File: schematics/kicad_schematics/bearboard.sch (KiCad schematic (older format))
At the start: 86 parts, among them P1 KOBICONN, P10 CONN_4, P11 CONN_10X2, P2 CONN_10X2, P3 CONN_10X2, P4 CONN_10X2, P5 CONN_10X2, P6 CONN_10X2, P7 CONN_10X2, P8 CONN_10X2, P9 CONN_7, SW1 SW_PUSH, SW5 SWITCH, SW6 SWITCH, U1 VBAT, U14 SD_CARD, U2 STM32F103, U3 TACT-SKQU, U4 EMA406GPS, X1 8-16MHz, X2 32.768KHz, X3 ARDUINOSHIELD

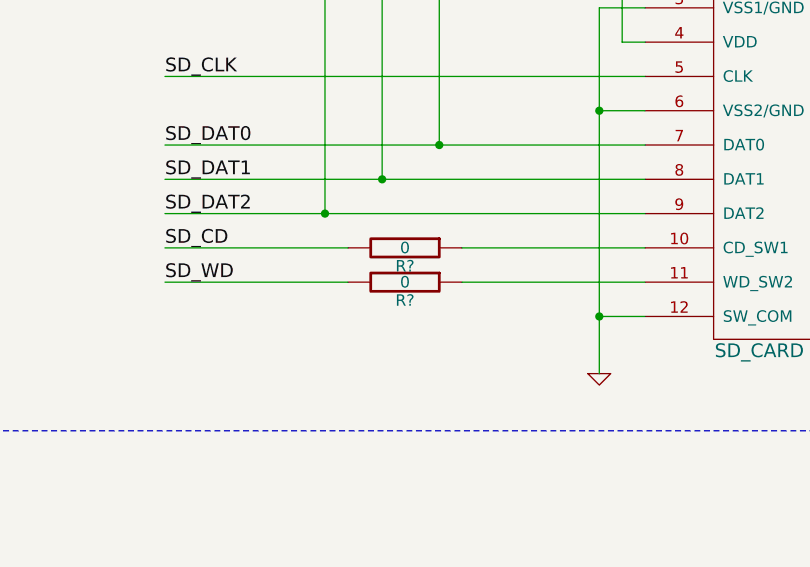
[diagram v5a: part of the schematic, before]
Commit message: added some more data sheets
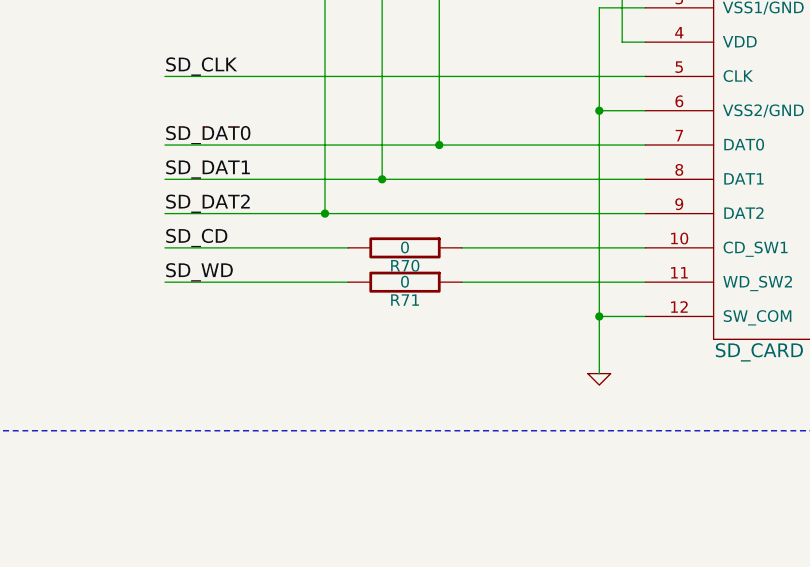
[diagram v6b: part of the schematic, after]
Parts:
- gave numbers to parts that had none: 2
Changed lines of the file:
@@
-EESchema Schematic File Version 2  date Sat 13 Mar 2010 12:50:25 PM EST
+EESchema Schematic File Version 2  date Sat 13 Mar 2010 02:28:46 PM EST
 LIBS:power
 LIBS:device
@@
 	18600 11050 17800 11050
 $Comp
-L R R?
+L R R71
 U 1 1 4B9BD03D
 P 18850 11200
-F 0 "R?" V 18930 11200 50  0000 C CNN
+F 0 "R71" V 18930 11200 50  0000 C CNN
 F 1 "0" V 18850 11200 50  0000 C CNN
 F 2 "SM0805" H 18850 11200 60  0001 C CNN
@@
 $EndComp
 $Comp
-L R R?
+L R R70
 U 1 1 4B9BD039
 P 18850 11050
-F 0 "R?" V 18930 11050 50  0000 C CNN
+F 0 "R70" V 18930 11050 50  0000 C CNN
 F 1 "0" V 18850 11050 50  0000 C CNN
 F 2 "SM0805" H 18850 11050 60  0001 C CNN
@@
 USB5V
 $Comp
-L 3V3 #PWR01
+L 3V3 #PWR31
 U 1 1 4B981769
 P 19800 8800
-F 0 "#PWR01" H 19800 8900 40  0001 C CNN
+F 0 "#PWR31" H 19800 8900 40  0001 C CNN
 F 1 "3V3" H 19800 8949 40  0000 C CNN
 	1    19800 8800
@@
 BOOT1
 $Comp
-L GND #PWR02
+L GND #PWR4
 U 1 1 4B980614
 P 750 3600
-F 0 "#PWR02" H 750 3600 30  0001 C CNN
+F 0 "#PWR4" H 750 3600 30  0001 C CNN
 F 1 "GND" H 750 3530 30  0001 C CNN
 	1    750  3600
@@
 $EndComp
 $Comp
-L 3V3 #PWR03
+L 3V3 #PWR3
 U 1 1 4B980612
 P 750 3350
-F 0 "#PWR03" H 750 3450 40  0001 C CNN
+F 0 "#PWR3" H 750 3450 40  0001 C CNN
 F 1 "3V3" H 750 3499 40  0000 C CNN
 	1    750  3350
@@
 $EndComp
 $Comp
-L 3V3 #PWR04
+L 3V3 #PWR1
 U 1 1 4B9805B2
 P 750 2650
-F 0 "#PWR04" H 750 2750 40  0001 C CNN
+F 0 "#PWR1" H 750 2750 40  0001 C CNN
 F 1 "3V3" H 750 2799 40  0000 C CNN
 	1    750  2650
@@
 POWER SUPPLY
 $Comp
-L 3V3 #PWR05
+L 3V3 #PWR16
 U 1 1 4B97F193
 P 5050 1250
-F 0 "#PWR05" H 5050 1350 40  0001 C CNN
+F 0 "#PWR16" H 5050 1350 40  0001 C CNN
 F 1 "3V3" H 5050 1399 40  0000 C CNN
 	1    5050 1250
@@
 VBAT
 $Comp
-L 3V3 #PWR06
+L 3V3 #PWR11
 U 1 1 4B97F11B
 P 1700 6150
-F 0 "#PWR06" H 1700 6250 40  0001 C CNN
+F 0 "#PWR11" H 1700 6250 40  0001 C CNN
 F 1 "3V3" H 1700 6299 40  0000 C CNN
 	1    1700 6150
@@
 JOY_UP
 $Comp
-L 3V3 #PWR07
+L 3V3 #PWR27
 U 1 1 4B97EDF8
 P 19000 6100
-F 0 "#PWR07" H 19000 6200 40  0001 C CNN
+F 0 "#PWR27" H 19000 6200 40  0001 C CNN
 F 1 "3V3" H 19000 6249 40  0000 C CNN
 	1    19000 6100
@@
 $EndComp
 $Comp
-L GND #PWR08
+L GND #PWR32
 U 1 1 4B97EDCC
 P 19850 7750
-F 0 "#PWR08" H 19850 7750 30  0001 C CNN
+F 0 "#PWR32" H 19850 7750 30  0001 C CNN
 F 1 "GND" H 19850 7680 30  0001 C CNN
 	1    19850 7750
@@
 $EndComp
 $Comp
-L GND #PWR09
+L GND #PWR28
 U 1 1 4B97D0B2
 P 19000 8250
-F 0 "#PWR09" H 19000 8250 30  0001 C CNN
+F 0 "#PWR28" H 19000 8250 30  0001 C CNN
 F 1 "GND" H 19000 8180 30  0001 C CNN
 	1    19000 8250
@@
 USART2_TX
 $Comp
-L GND #PWR010
+L GND #PWR18
 U 1 1 4B97C2CE
 P 5950 6150
-F 0 "#PWR010" H 5950 6150 30  0001 C CNN
+F 0 "#PWR18" H 5950 6150 30  0001 C CNN
 F 1 "GND" H 5950 6080 30  0001 C CNN
 	1    5950 6150
@@
 $EndComp
 $Comp
-L GND #PWR011
+L GND #PWR9
 U 1 1 4B97BC68
 P 1500 1500
-F 0 "#PWR011" H 1500 1500 30  0001 C CNN
+F 0 "#PWR9" H 1500 1500 30  0001 C CNN
 F 1 "GND" H 1500 1430 30  0001 C CNN
 	1    1500 1500
@@
 SD CARD INTERFACE
 $Comp
-L GND #PWR012
+L GND #PWR22
 U 1 1 4B91D59F
 P 11950 13550
-F 0 "#PWR012" H 11950 13550 30  0001 C CNN
+F 0 "#PWR22" H 11950 13550 30  0001 C CNN
 F 1 "GND" H 11950 13480 30  0001 C CNN
 	1    11950 13550
@@
 $EndComp
 $Comp
-L GND #PWR013
+L GND #PWR23
 U 1 1 4B91D596
 P 13250 13300
-F 0 "#PWR013" H 13250 13300 30  0001 C CNN
+F 0 "#PWR23" H 13250 13300 30  0001 C CNN
 F 1 "GND" H 13250 13230 30  0001 C CNN
 	1    13250 13300
@@
 $EndComp
 $Comp
-L 3V3 #PWR014
+L 3V3 #PWR25
 U 1 1 4B918558
 P 18600 4250
-F 0 "#PWR014" H 18600 4350 40  0001 C CNN
+F 0 "#PWR25" H 18600 4350 40  0001 C CNN
 F 1 "3V3" H 18600 4399 40  0000 C CNN
 	1    18600 4250
@@
 $EndComp
 $Comp
-L GND #PWR015
+L GND #PWR2
 U 1 1 4B918557
 P 750 2900
-F 0 "#PWR015" H 750 2900 30  0001 C CNN
+F 0 "#PWR2" H 750 2900 30  0001 C CNN
 F 1 "GND" H 750 2830 30  0001 C CNN
 	1    750  2900
@@
 5V0
 $Comp
-L GND #PWR016
+L GND #PWR24
 U 1 1 4B906F37
 P 13600 10900
-F 0 "#PWR016" H 13600 10900 30  0001 C CNN
+F 0 "#PWR24" H 13600 10900 30  0001 C CNN
 F 1 "GND" H 13600 10830 30  0001 C CNN
 	1    13600 10900
@@
 VDDA
 $Comp
-L GND #PWR017
+L GND #PWR8
 U 1 1 4B906833
 P 1400 7850
-F 0 "#PWR017" H 1400 7850 30  0001 C CNN
+F 0 "#PWR8" H 1400 7850 30  0001 C CNN
 F 1 "GND" H 1400 7780 30  0001 C CNN
 	1    1400 7850
@@
 $EndComp
 $Comp
-L 3V3 #PWR018
+L 3V3 #PWR5
 U 1 1 4B906827
 P 750 7300
-F 0 "#PWR018" H 750 7400 40  0001 C CNN
+F 0 "#PWR5" H 750 7400 40  0001 C CNN
 F 1 "3V3" H 750 7449 40  0000 C CNN
 	1    750  7300
@@
 $EndComp
 $Comp
-L GND #PWR019
+L GND #PWR13
 U 1 1 4B906768
 P 2800 8250
-F 0 "#PWR019" H 2800 8250 30  0001 C CNN
+F 0 "#PWR13" H 2800 8250 30  0001 C CNN
 F 1 "GND" H 2800 8180 30  0001 C CNN
 	1    2800 8250
@@
 $EndComp
 $Comp
-L GND #PWR020
+L GND #PWR12
 U 1 1 4B906595
 P 1700 6700
-F 0 "#PWR020" H 1700 6700 30  0001 C CNN
+F 0 "#PWR12" H 1700 6700 30  0001 C CNN
 F 1 "GND" H 1700 6630 30  0001 C CNN
 	1    1700 6700
@@
 $EndComp
 $Comp
-L 3V3 #PWR021
+L 3V3 #PWR21
 U 1 1 4B906233
 P 9300 12950
-F 0 "#PWR021" H 9300 13050 40  0001 C CNN
+F 0 "#PWR21" H 9300 13050 40  0001 C CNN
 F 1 "3V3" H 9300 13099 40  0000 C CNN
 	1    9300 12950
@@
 $EndComp
 $Comp
-L 3V3 #PWR022
+L 3V3 #PWR10
 U 1 1 4B905C37
 P 1550 4350
-F 0 "#PWR022" H 1550 4450 40  0001 C CNN
+F 0 "#PWR10" H 1550 4450 40  0001 C CNN
 F 1 "3V3" H 1550 4499 40  0000 C CNN
 	1    1550 4350
@@
 $EndComp
 $Comp
-L 3V3 #PWR023
+L 3V3 #PWR19
 U 1 1 4B9034AD
 P 8100 14100
-F 0 "#PWR023" H 8100 14200 40  0001 C CNN
+F 0 "#PWR19" H 8100 14200 40  0001 C CNN
 F 1 "3V3" H 8100 14249 40  0000 C CNN
 	1    8100 14100
@@
 TMS/SWDIO
 $Comp
-L GND #PWR024
+L GND #PWR20
 U 1 1 4B903530
 P 8100 15950
-F 0 "#PWR024" H 8100 15950 30  0001 C CNN
+F 0 "#PWR20" H 8100 15950 30  0001 C CNN
 F 1 "GND" H 8100 15880 30  0001 C CNN
 	1    8100 15950
@@
 GND
 $Comp
-L GND #PWR025
+L GND #PWR6
 U 1 1 4B9032D4
 P 850 5450
-F 0 "#PWR025" H 850 5450 30  0001 C CNN
+F 0 "#PWR6" H 850 5450 30  0001 C CNN
 F 1 "GND" H 850 5380 30  0001 C CNN
 	1    850  5450
@@
 RESET#
 $Comp
-L 3V3 #PWR026
+L 3V3 #PWR26
 U 1 1 4B903136
 P 18650 1750
-F 0 "#PWR026" H 18650 1850 40  0001 C CNN
+F 0 "#PWR26" H 18650 1850 40  0001 C CNN
 F 1 "3V3" H 18650 1899 40  0000 C CNN
 	1    18650 1750
@@
 FSMC_NOE
 $Comp
-L GND #PWR027
+L GND #PWR15
 U 1 1 4B9001FC
 P 3500 1700
-F 0 "#PWR027" H 3500 1700 30  0001 C CNN
+F 0 "#PWR15" H 3500 1700 30  0001 C CNN
 F 1 "GND" H 3500 1630 30  0001 C CNN
 	1    3500 1700
@@
 $EndComp
 $Comp
-L +5V #PWR028
+L +5V #PWR17
 U 1 1 4B9001CE
 P 5300 1250
-F 0 "#PWR028" H 5300 1340 20  0001 C CNN
+F 0 "#PWR17" H 5300 1340 20  0001 C CNN
 F 1 "+5V" H 5300 1340 30  0000 C CNN
 	1    5300 1250
@@
 $EndComp
 $Comp
-L GND #PWR029
+L GND #PWR14
 U 1 1 4B7EA0B9
 P 3000 10700
-F 0 "#PWR029" H 3000 10700 30  0001 C CNN
+F 0 "#PWR14" H 3000 10700 30  0001 C CNN
 F 1 "GND" H 3000 10630 30  0001 C CNN
 	1    3000 10700
@@
 $EndComp
 $Comp
-L GND #PWR030
+L GND #PWR7
 U 1 1 4B7E9BE8
 P 1350 10750
-F 0 "#PWR030" H 1350 10750 30  0001 C CNN
+F 0 "#PWR7" H 1350 10750 30  0001 C CNN
 F 1 "GND" H 1350 10680 30  0001 C CNN
 	1    1350 10750
@@
 SD_DAT3
 $Comp
-L GND #PWR031
+L GND #PWR30
 U 1 1 4B7E2670
 P 19700 11600
-F 0 "#PWR031" H 19700 11600 30  0001 C CNN
+F 0 "#PWR30" H 19700 11600 30  0001 C CNN
 F 1 "GND" H 19700 11530 30  0001 C CNN
 	1    19700 11600
@@
 $EndComp
 $Comp
-L 3V3 #PWR032
+L 3V3 #PWR29
 U 1 1 4B7E255C
 P 19000 8800
-F 0 "#PWR032" H 19000 8900 40  0001 C CNN
+F 0 "#PWR29" H 19000 8900 40  0001 C CNN
 F 1 "3V3" H 19000 8949 40  0000 C CNN
 	1    19000 8800

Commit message: added npn datasheet
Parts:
- D1, D2, D3: footprint (none) -> SC-59
- L1: footprint (none) -> SM0805
- P1: footprint (none) -> PowerConnector
- U1: footprint (none) -> 2998_bat_holder
- X2: footprint (none) -> 32_768kHz_Crystal
- X3: footprint (none) -> arduino_sheild
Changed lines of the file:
@@
-EESchema Schematic File Version 2  date Sat 13 Mar 2010 03:45:55 PM EST
+EESchema Schematic File Version 2  date Sat 13 Mar 2010 04:13:45 PM EST
 LIBS:power
 LIBS:device
@@
 F 0 "P1" H 900 950 50  0000 L BNN
 F 1 "KOBICONN" H 750 1350 50  0000 L BNN
+F 2 "PowerConnector" H 750 1250 60  0001 C CNN
 	1    750  1250
 	1    0    0    -1
@@
 F 0 "D1" H 2900 1150 40  0000 C CNN
 F 1 "DIODESCH" H 2900 950 40  0000 C CNN
+F 2 "SC-59" H 2900 1050 60  0001 C CNN
 	1    2900 1050
 	1    0    0    -1
@@
 F 0 "X3" H 12850 16000 60  0000 C CNN
 F 1 "ARDUINOSHIELD" H 13250 14100 60  0000 C CNN
+F 2 "arduino_sheild" H 13200 15050 60  0001 C CNN
 	1    13200 15050
 	1    0    0    -1
@@
 F 0 "L1" V 1000 7350 40  0000 C CNN
 F 1 "BEAD" V 1150 7350 40  0000 C CNN
+F 2 "SM0805" H 1050 7350 60  0001 C CNN
 	1    1050 7350
 	0    1    1    0
@@
 F 0 "U1" H 750 6700 60  0000 C CNN
 F 1 "VBAT" H 850 6250 60  0000 C CNN
+F 2 "2998_bat_holder" H 1000 6500 60  0001 C CNN
 	1    1000 6500
 	1    0    0    -1
@@
 F 0 "D2" H 2900 1450 40  0000 C CNN
 F 1 "DIODESCH" H 2900 1250 40  0000 C CNN
+F 2 "SC-59" H 2900 1350 60  0001 C CNN
 	1    2900 1350
 	1    0    0    -1
@@
 F 0 "D3" H 2900 1750 40  0000 C CNN
 F 1 "DIODESCH" H 2900 1550 40  0000 C CNN
+F 2 "SC-59" H 2900 1650 60  0001 C CNN
 	1    2900 1650
 	1    0    0    -1
@@
 F 0 "X2" H 3000 10200 60  0000 C CNN
 F 1 "32.768KHz" H 3000 9900 60  0000 C CNN
+F 2 "32_768kHz_Crystal" H 3000 10050 60  0001 C CNN
 	1    3000 10050
 	1    0    0    -1
